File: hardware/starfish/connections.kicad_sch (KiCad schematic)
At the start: 21 parts, among them J1 INS, J10 Stemma QT, J2 8P8C_LED_Shielded, J3 CAM, J4 CAMLED, J5 OUT1, J6 BLTOUCH, U5 74HC2G34, U6 TVS, U7 74HC2G34

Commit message: First pass at schematic for starfish
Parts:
- removed J10: Stemma QT, Connector_JST:JST_SH_SM04B-SRSS-TB_1x04-1MP_P1.00mm_Horizontal, symbol Connector_Generic_MountingPin:Conn_01x04_MountingPin
- removed J2: 8P8C_LED_Shielded, winterbloom:RJ45_Amphenol_RJE45-188-1411_Vertical, symbol Connector:8P8C_LED_Shielded
- removed J3: CAM, Connector_JST:JST_SH_SM04B-SRSS-TB_1x04-1MP_P1.00mm_Horizontal, symbol Connector_Generic_MountingPin:Conn_01x04_MountingPin
- removed J6: BLTOUCH, Connector_JST:JST_SH_SM05B-SRSS-TB_1x05-1MP_P1.00mm_Horizontal, symbol Connector_Generic_MountingPin:Conn_01x05_MountingPin
- removed R1, R15, R2, R26, R27: 5.1k, Resistor_SMD:R_0402_1005Metric_Pad0.72x0.64mm_HandSolder, symbol Device:R_US
- added D401, D402, D403, D404: TVS, symbol Device:D_TVS_Filled
- added D405: 30V, winterbloom:D_SOD-123, symbol Device:D_Schottky_Filled
- added J403: Voltage, symbol Connector_Generic:Conn_01x03
- added J405, J406: Qwiic, Connector_JST:JST_SH_SM04B-SRSS-TB_1x04-1MP_P1.00mm_Horizontal, symbol Connector_Generic_MountingPin:Conn_01x04_MountingPin
- added J407: USB B, winterbloom:USB_B_Receptacle, symbol winterbloom:USB_B_Receptacle
- J401: renamed from J4; value CAMLED -> CAM LED
- J402: renamed from J5; value OUT1 -> AUX OUT
- J404: renamed from J1; value INS -> INPUTS
- renumbered C27 to C401, C1 to C402, R13 to R401, R14 to R402, R3 to R403, R16 to R404, U7 to U401, U5 to U402, U6 to U403
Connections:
- net +3V3: now also J403.1 (Pin_1), J405.2 (Pin_2), J406.2 (Pin_2)
- net +5V: now also D405.1 (K), J403.3 (Pin_3); no longer J404.1 (Pin_1), U403.5 (VBUS)
- net GND: now also D401.1 (A1), D402.1 (A1), D403.1 (A1), D404.1 (A1), J405.1 (Pin_1), J405.MP (MountPin), J406.1 (Pin_1), J406.MP (MountPin), J407.4 (GND), J407.5 (Shield)
- net MCU_D+: now also J407.3 (D+)
- net MCU_D-: now also J407.2 (D-)
- net AUX OUT: now reaches J402.1 (Pin_1), U401.4 (2Y)
- net CAM LED OUT: now reaches J401.1 (Pin_1), U401.6 (1Y)
- new net: D403.2 (A2), J405.4 (Pin_4)
- new net: D405.2 (A), J407.1 (VBUS), U403.5 (VBUS)
- new net: J403.2 (Pin_2), J404.1 (Pin_1)
- new net QWIIC1_SDA: D401.2 (A2), J405.3 (Pin_3)
- new net QWIIC2_SCK: D404.2 (A2), J406.4 (Pin_4)
- new net QWIIC2_SDA: D402.2 (A2), J406.3 (Pin_3)
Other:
- note added: "Qwiic"
- note added: "USB"
- note added: "Voltage selectable between 3.3V and 5V"
- note removed: "* Make sure TVS diodes are close to J1 * Route camera USB pair over uninterrupted ground plane * Note twisted pair wiring on Cat6 cable: 1. White/Green 2. Green 3. White/Orange 4. Blue 5. White/Blue 6. Orange 7. White/Brown 8. Brown"
- note removed: "Black"
- note removed: "Brown"
- note removed: "CAT6, USB TVS, and camera header"
- note removed: "Red"
- note removed: "TODO: double check pinout"
- note removed: "White"
- note removed: "Yellow"
- title: Jellyfish -> Starfish
- moved on the sheet: C401, C402, J401, J402, J404, R401, R402, R403, R404, U401, U402, U403

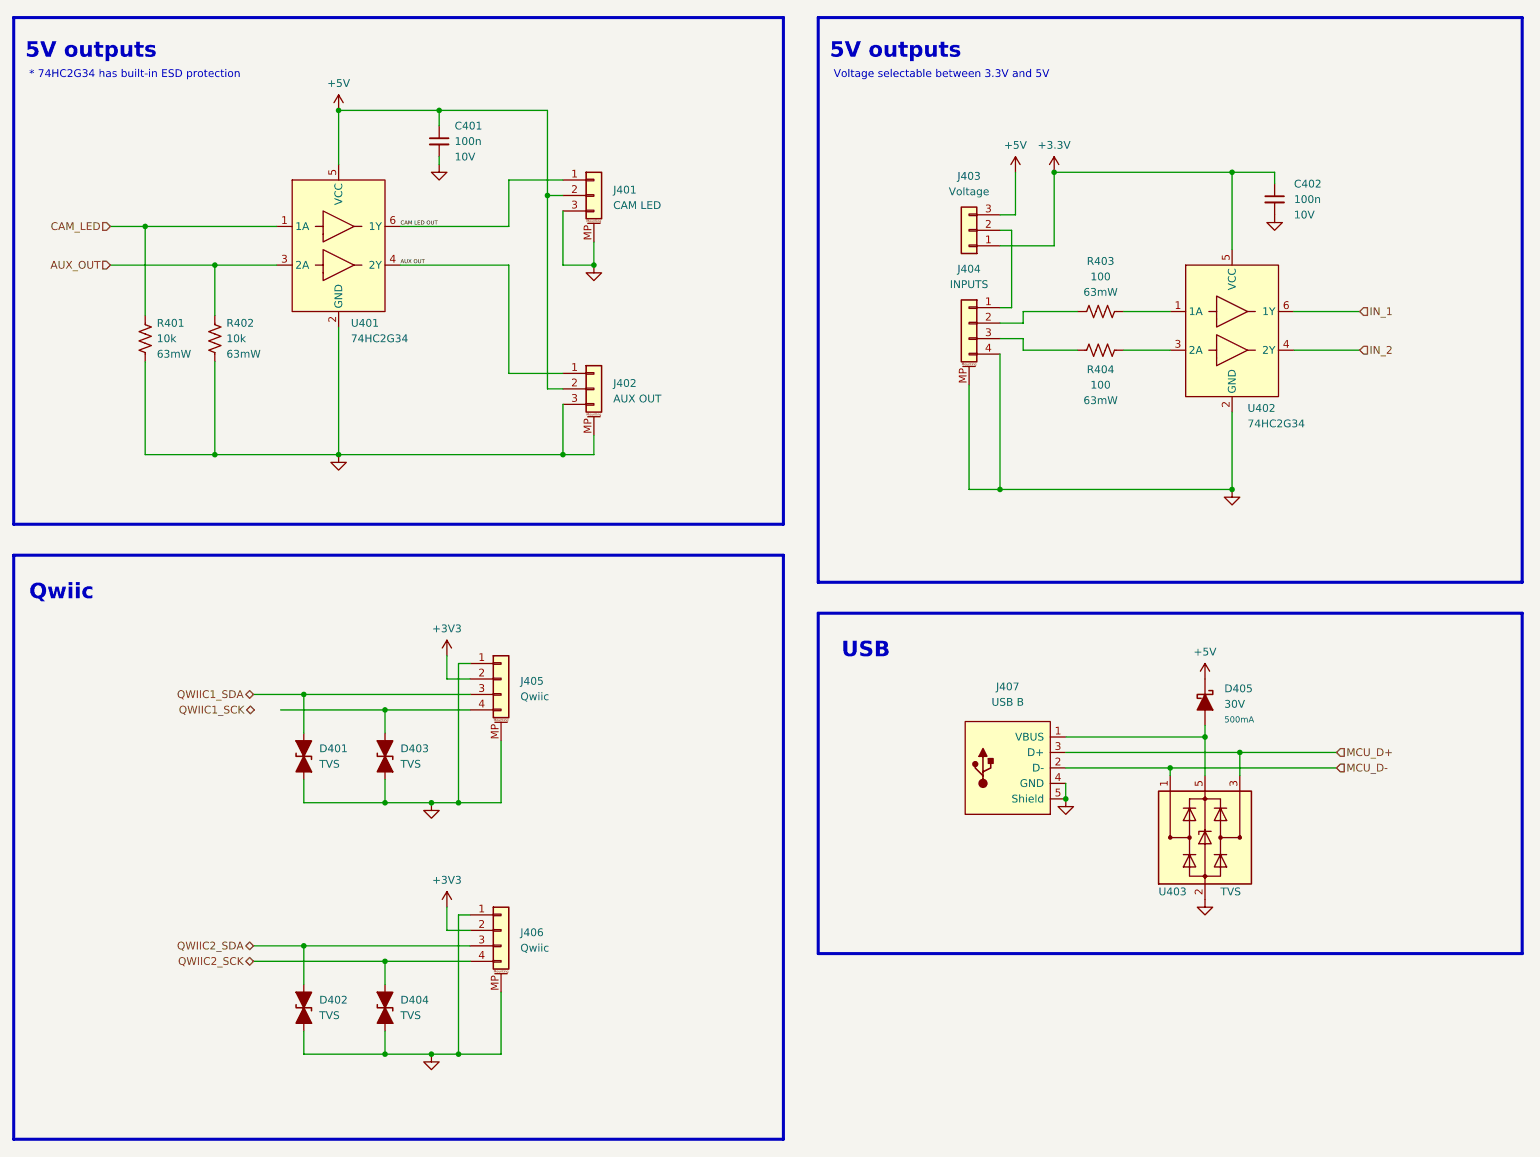
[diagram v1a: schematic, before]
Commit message: Mostly finished starfish schematic, ready for layout!
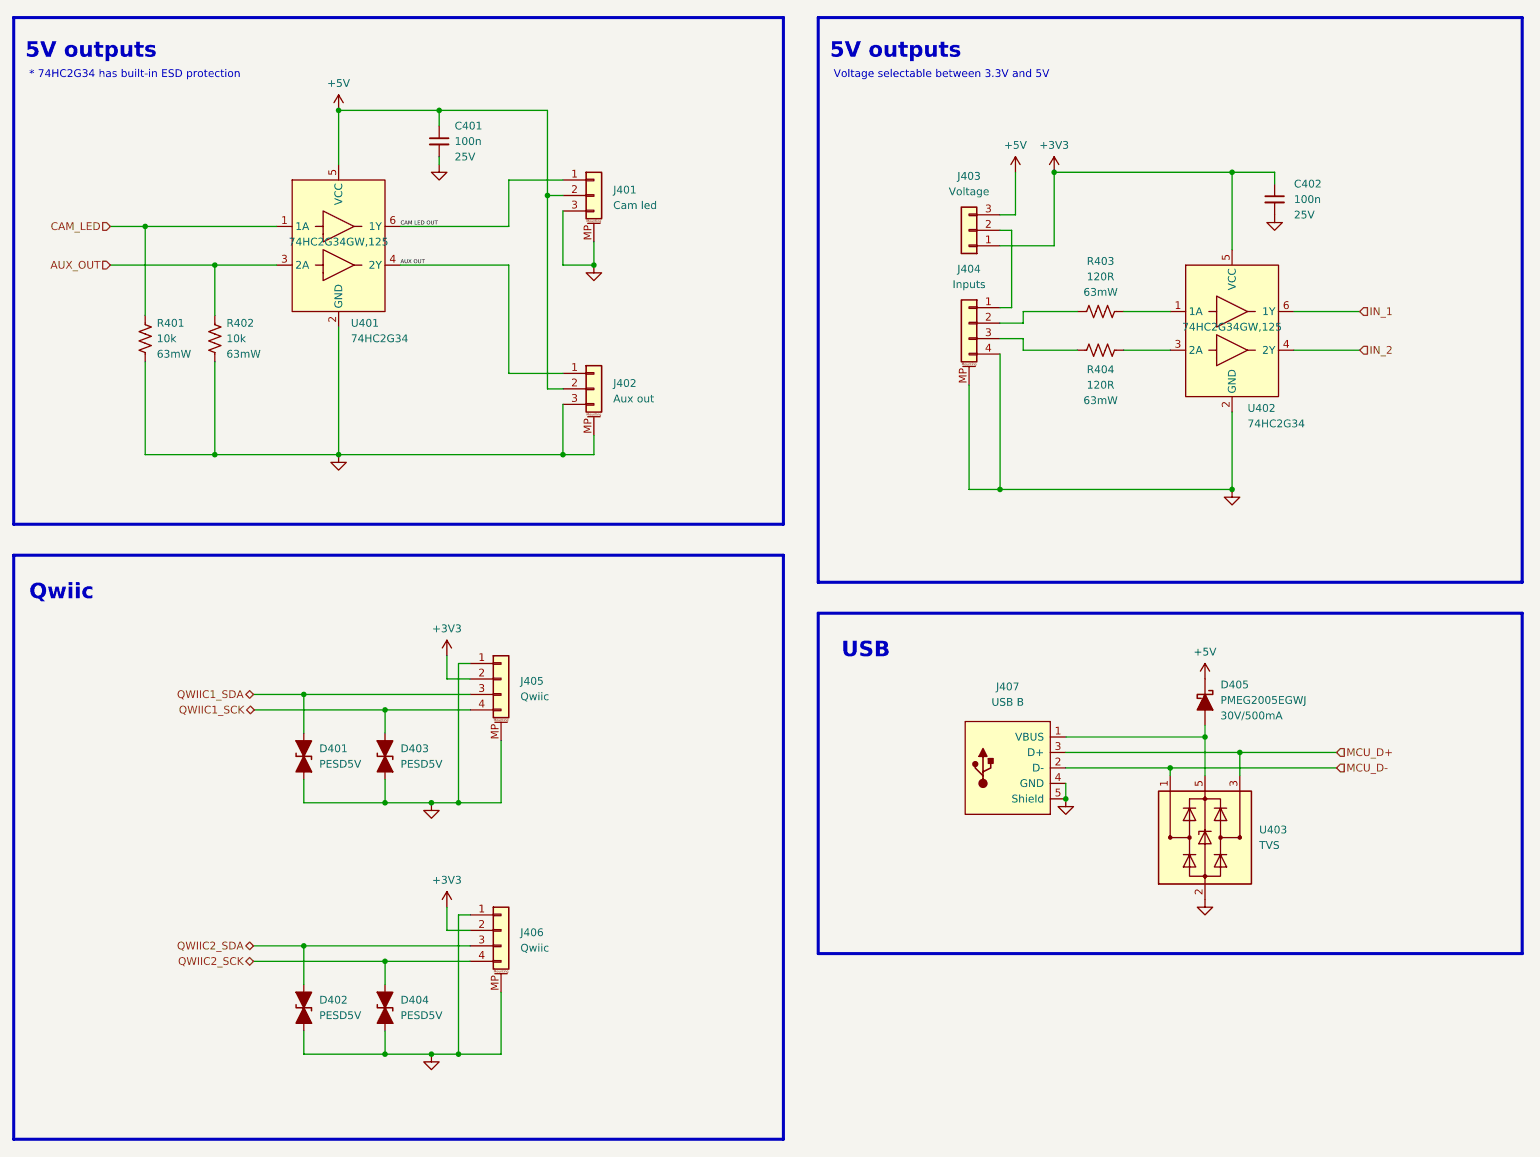
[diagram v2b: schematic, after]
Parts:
- C401, C402: footprint Capacitor_SMD:C_0402_1005Metric_Pad0.74x0.62mm_HandSolder -> winterbloom:C_0402_HandSolder; Rating 10V -> 25V
- D401, D402, D403, D404: value TVS -> PESD5V; footprint (none) -> Package_TO_SOT_SMD:SOT-23; Notes (none) -> DOUBLE CHECK FOOTPRINT; Rating (none) -> TVS
- D405: value 30V -> PMEG2005EGWJ; MPN PMEG2005EGWJ, PMEG3005EGWX -> (none); Rating 500mA -> 30V/500mA; mpn (none) -> PMEG2005EGWJ, PMEG3005EGWX
- J401: value CAM LED -> Cam led
- J402: value AUX OUT -> Aux out
- J403: footprint (none) -> Connector_PinHeader_2.54mm:PinHeader_1x02_P2.54mm_Vertical
- J404: value INPUTS -> Inputs; footprint Connector_JST:JST_SH_SM04B-SRSS-TB_1x04-1MP_P1.00mm_Horizontal -> Connector_PinHeader_2.54mm:PinHeader_1x04_P2.54mm_Vertical
- J407: MPN 5787834-1 -> (none); mpn (none) -> 5787834-1
- R401, R402: footprint Resistor_SMD:R_0402_1005Metric_Pad0.72x0.64mm_HandSolder -> winterbloom:R_0402_HandSolder
- R403, R404: value 100 -> 120R; footprint Resistor_SMD:R_0402_1005Metric_Pad0.72x0.64mm_HandSolder -> winterbloom:R_0402_HandSolder; mpn RC0402JR-0710KL -> (none)
- U401, U402: MPN (none) -> 74HC2G34GW,125
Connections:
- net QWIIC1_SCK: now also D403.2 (A2), J405.4 (Pin_4)

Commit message: First pass at layout and routing
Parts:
- removed J401: Cam led, Connector_JST:JST_SH_SM03B-SRSS-TB_1x03-1MP_P1.00mm_Horizontal, symbol Connector_Generic_MountingPin:Conn_01x03_MountingPin
- removed J402: Aux out, Connector_JST:JST_SH_SM03B-SRSS-TB_1x03-1MP_P1.00mm_Horizontal, symbol Connector_Generic_MountingPin:Conn_01x03_MountingPin
- removed J404: Inputs, Connector_PinHeader_2.54mm:PinHeader_1x04_P2.54mm_Vertical, symbol Connector_Generic_MountingPin:Conn_01x04_MountingPin
- added D406: USB, winterbloom:LED_0805_Kingbright_APT2012, symbol Device:LED_Filled
- added J401: Cam LED, Connector_JST:JST_XH_B3B-XH-AM_1x03_P2.50mm_Vertical, symbol Connector_Generic:Conn_01x03
- added J402: Aux out, Connector_JST:JST_XH_B3B-XH-AM_1x03_P2.50mm_Vertical, symbol Connector_Generic:Conn_01x03
- added J404: Inputs, Connector_JST:JST_XH_B4B-XH-AM_1x04_P2.50mm_Vertical, symbol Connector_Generic:Conn_01x04
- added R405: 1k, winterbloom:R_0402_HandSolder, symbol Device:R_US
- D401, D402, D403, D404: footprint Package_TO_SOT_SMD:SOT-23 -> winterbloom:D_SOD-323; MPN (none) -> PESD5V0U1BA,115
- J403: footprint Connector_PinHeader_2.54mm:PinHeader_1x02_P2.54mm_Vertical -> Connector_PinHeader_2.54mm:PinHeader_1x03_P2.54mm_Vertical
- J407: footprint winterbloom:USB_B_Receptacle -> winterbloom:USB_B_Receptacle_Horizontal; mpn 5787834-1 -> (none)
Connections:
- net +5V: now also J401.2 (Pin_2), J402.2 (Pin_2)
- net AUX OUT: now also J402.1 (Pin_1)
- net CAM LED OUT: now also J401.1 (Pin_1)
- net GND: now also J401.3 (Pin_3), J402.3 (Pin_3), J404.4 (Pin_4), R405.2
- net MCU_D+: now also U403.1 (D-), U403.6 (D-); no longer U403.3 (D+), U403.4 (D+)
- net MCU_D-: now also U403.3 (D+), U403.4 (D+); no longer U403.1 (D-), U403.6 (D-)
- net at R404.2: now also J404.3 (Pin_3)
- net at D405.2 (A), J407.1 (VBUS), U403.5 (VBUS): now also D406.2 (A)
- net at J403.2 (Pin_2): now also J404.1 (Pin_1)
- net at R403.2: now also J404.2 (Pin_2)
- new net: D406.1 (K), R405.1
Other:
- moved on the sheet: D405, J407, U403

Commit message: Layout and routing mostly done! Just gotta make it prettier!
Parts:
- J401, J402: footprint Connector_JST:JST_XH_B3B-XH-AM_1x03_P2.50mm_Vertical -> winterbloom:JST_XH_B3B-XH-AM_1x03_P2.50mm_Vertical
- J404: footprint Connector_JST:JST_XH_B4B-XH-AM_1x04_P2.50mm_Vertical -> winterbloom:JST_XH_B4B-XH-AM_1x04_P2.50mm_Vertical
- J405, J406: footprint Connector_JST:JST_SH_SM04B-SRSS-TB_1x04-1MP_P1.00mm_Horizontal -> winterbloom:JST_SH_SM04B-SRSS-TB_1x04-1MP_P1.00mm_Horizontal
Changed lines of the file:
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@@
       (effects (font (size 1.27 1.27)) (justify left))
     )
-    (property "Footprint" "Connector_JST:JST_XH_B3B-XH-AM_1x03_P2.50mm_Vertical" (id 2) (at 110.49 76.835 0)
+    (property "Footprint" "winterbloom:JST_XH_B3B-XH-AM_1x03_P2.50mm_Vertical" (id 2) (at 110.49 76.835 0)
       (effects (font (size 1.27 1.27)) hide)
     )
@@
       (effects (font (size 1.27 1.27)) (justify left))
     )
-    (property "Footprint" "Connector_JST:JST_XH_B3B-XH-AM_1x03_P2.50mm_Vertical" (id 2) (at 110.49 45.085 0)
+    (property "Footprint" "winterbloom:JST_XH_B3B-XH-AM_1x03_P2.50mm_Vertical" (id 2) (at 110.49 45.085 0)
       (effects (font (size 1.27 1.27)) hide)
     )
@@
       (effects (font (size 1.27 1.27)) (justify left))
     )
-    (property "Footprint" "Connector_JST:JST_SH_SM04B-SRSS-TB_1x04-1MP_P1.00mm_Horizontal" (id 2) (at 95.25 165.735 0)
+    (property "Footprint" "winterbloom:JST_SH_SM04B-SRSS-TB_1x04-1MP_P1.00mm_Horizontal" (id 2) (at 95.25 165.735 0)
       (effects (font (size 1.27 1.27)) hide)
     )
@@
     (property "Reference" "J404" (id 0) (at 172.085 57.15 0))
     (property "Value" "Inputs" (id 1) (at 172.085 59.69 0))
-    (property "Footprint" "Connector_JST:JST_XH_B4B-XH-AM_1x04_P2.50mm_Vertical" (id 2) (at 172.085 66.04 0)
+    (property "Footprint" "winterbloom:JST_XH_B4B-XH-AM_1x04_P2.50mm_Vertical" (id 2) (at 172.085 66.04 0)
       (effects (font (size 1.27 1.27)) hide)
     )
@@
       (effects (font (size 1.27 1.27)) (justify left))
     )
-    (property "Footprint" "Connector_JST:JST_SH_SM04B-SRSS-TB_1x04-1MP_P1.00mm_Horizontal" (id 2) (at 95.25 124.46 0)
-      (effects (font (size 1.27 1.27)) hide)
-    )
+    (property "Footprint" "winterbloom:JST_SH_SM04B-SRSS-TB_1x04-1MP_P1.00mm_Horizontal" (id 2) (at 95.25 124.46 0)
+      (effects (font (size 1.27 1.27)) hide)
+    )
